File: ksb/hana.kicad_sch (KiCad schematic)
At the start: 19 parts, among them U4 X850744-001

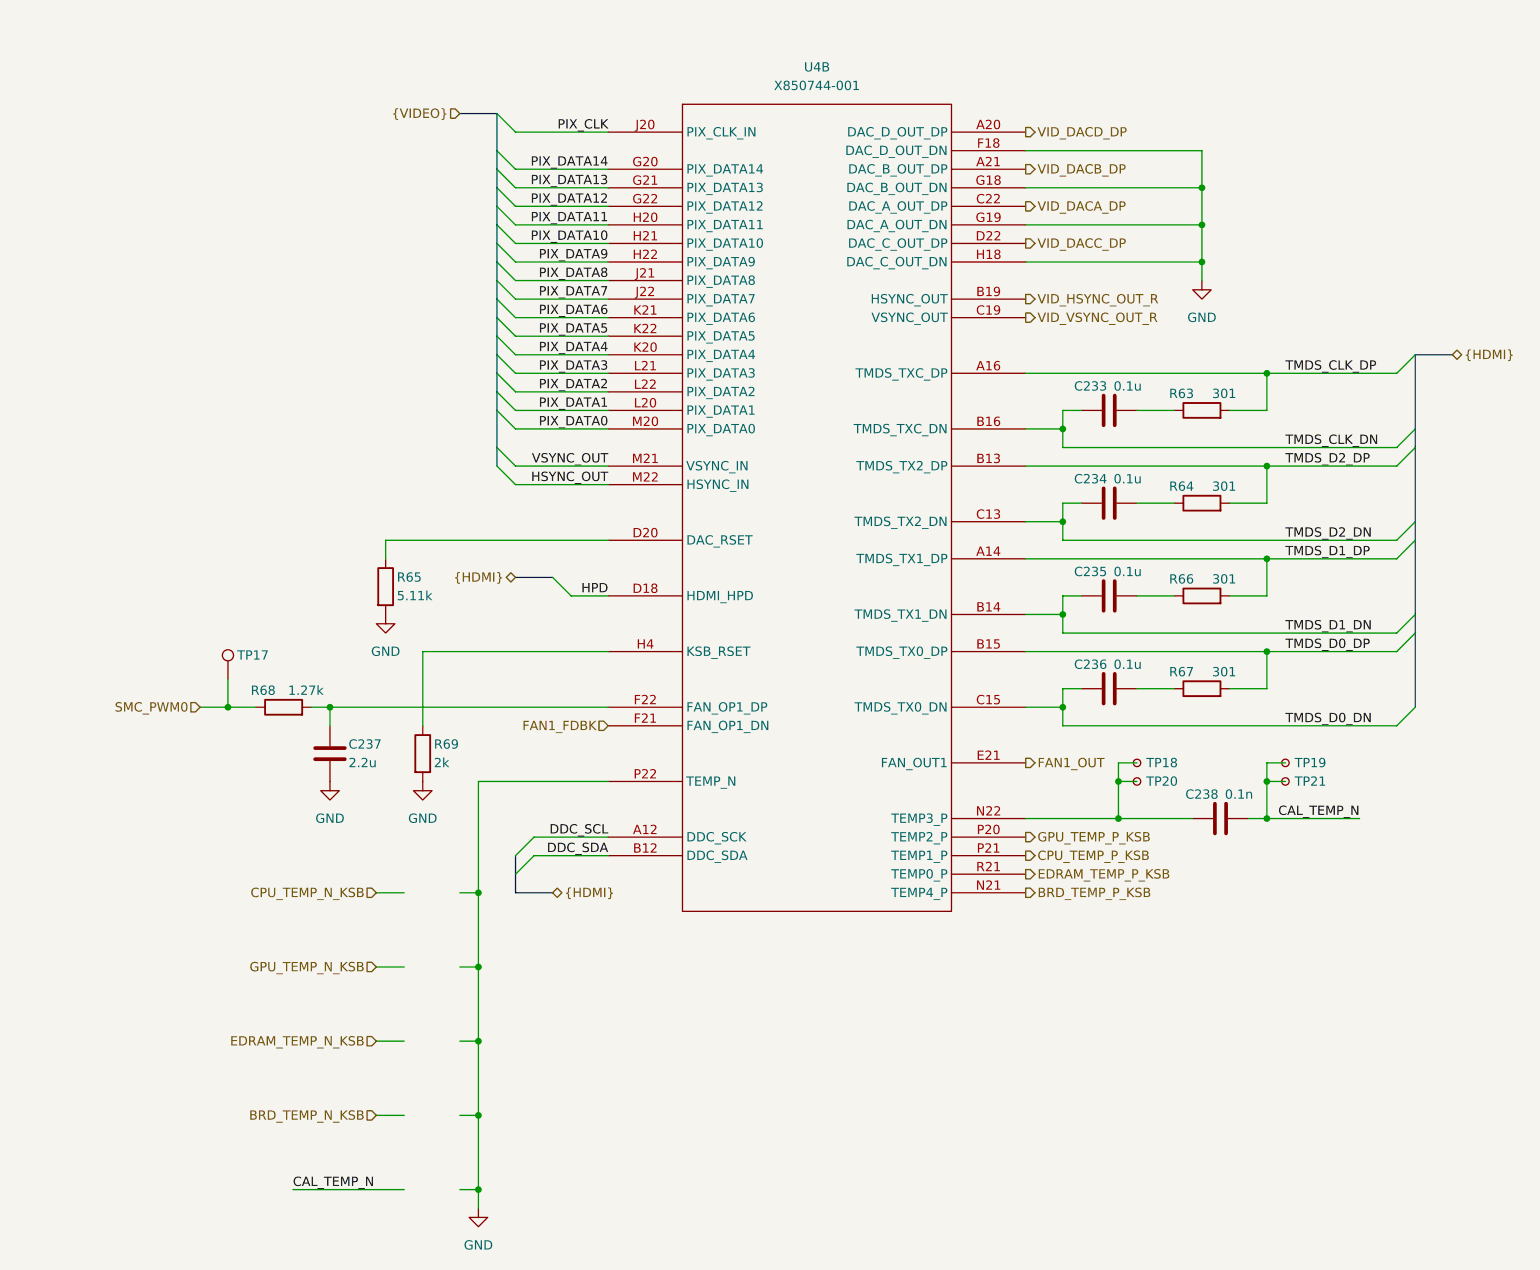
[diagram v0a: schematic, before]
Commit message: Cleanup, SMC GPIO connections and Temperature sensing
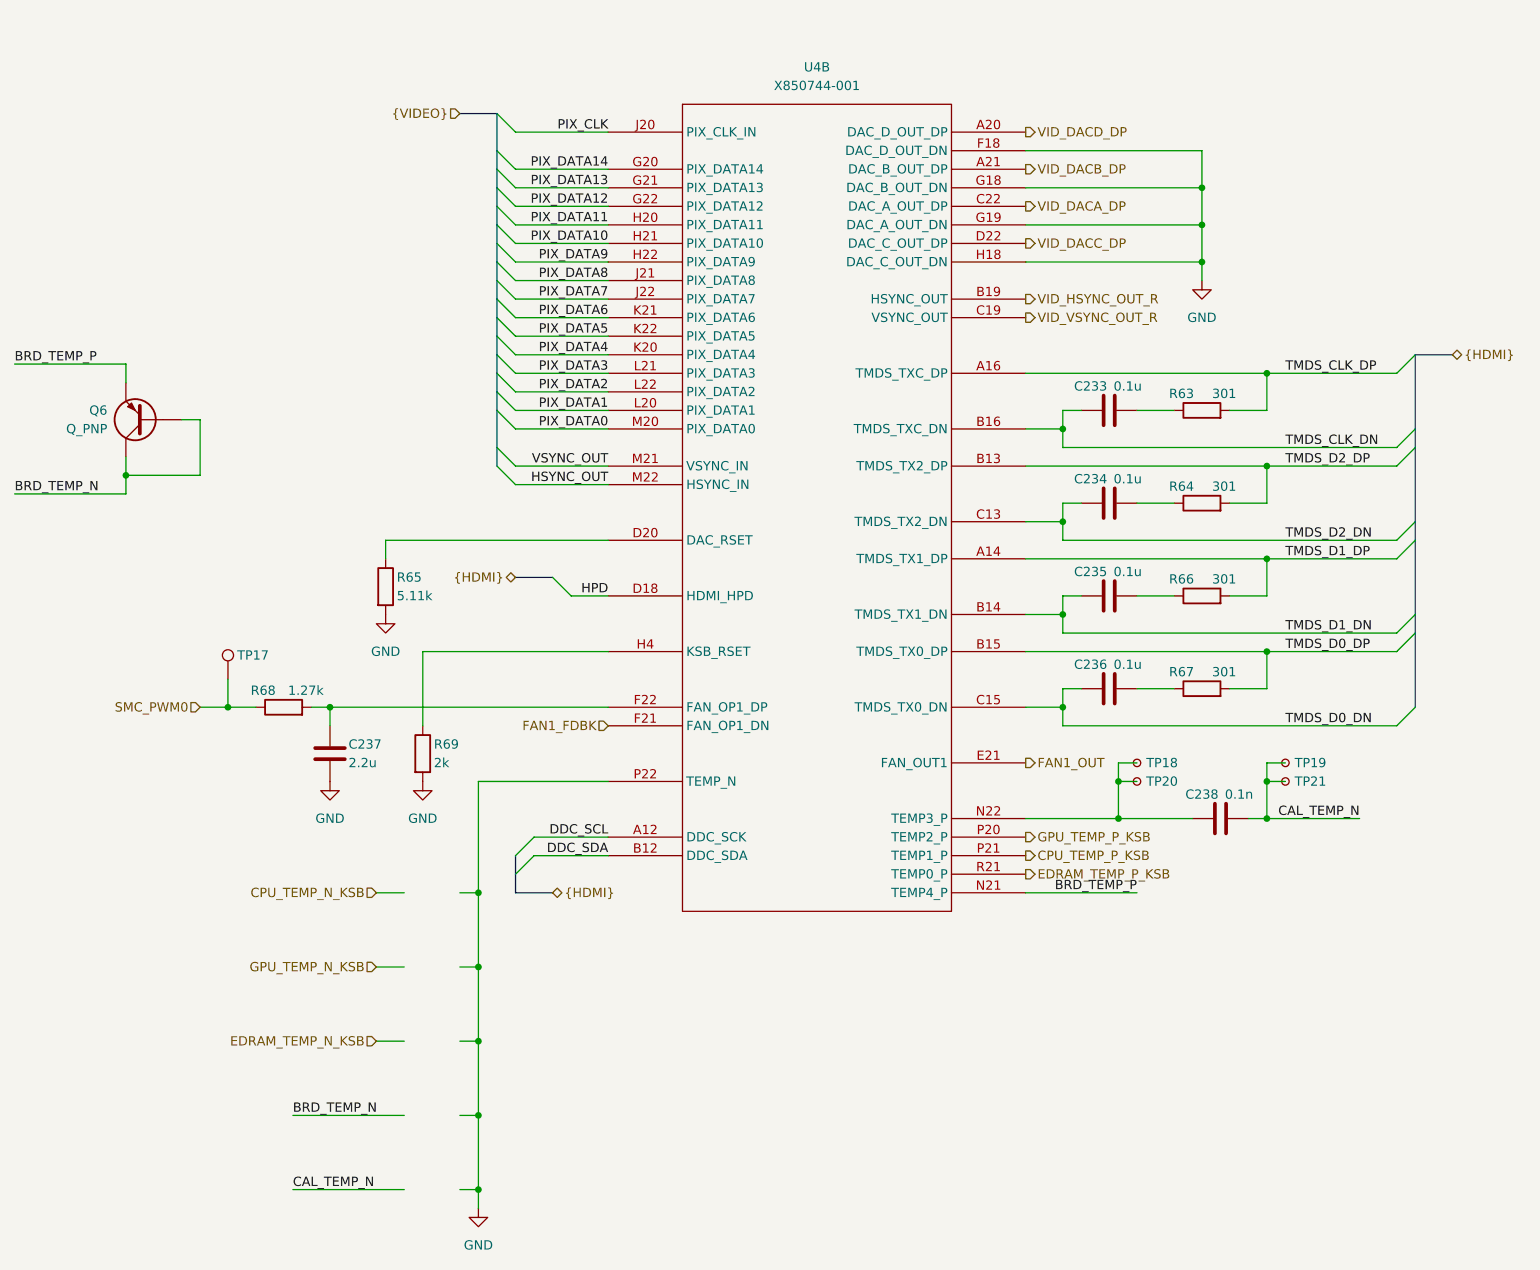
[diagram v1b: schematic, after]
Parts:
- added Q6: Q_PNP, symbol Device:Q_PNP
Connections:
- net BRD_TEMP_P_KSB renamed BRD_TEMP_P
- net BRD_TEMP_P: now also Q6.E
- new net BRD_TEMP_N: Q6.B, Q6.C
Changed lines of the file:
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@@
+	)
+	(junction
+		(at 53.34 80.01)
+		(diameter 0)
+		(color 0 0 0 0)
 	)
 	(junction
@@
 	(wire
 		(pts
-			(xy 87.63 167.64) (xy 91.44 167.64)
-		)
-		(stroke
-			(width 0)
-			(type default)
-		)
-	)
-	(wire
-		(pts
 			(xy 181.61 109.22) (xy 184.15 109.22)
 		)
@@
 	(wire
 		(pts
+			(xy 176.53 137.16) (xy 191.77 137.16)
+		)
+		(stroke
+			(width 0)
+			(type default)
+		)
+	)
+	(wire
+		(pts
 			(xy 209.55 121.92) (xy 212.09 121.92)
 		)
@@
 		)
 	)
+	(wire
+		(pts
+			(xy 53.34 64.77) (xy 53.34 67.31)
+		)
+		(stroke
+			(width 0)
+			(type default)
+		)
+	)
 	(bus
 		(pts
@@
 	(wire
 		(pts
+			(xy 76.2 167.64) (xy 91.44 167.64)
+		)
+		(stroke
+			(width 0)
+			(type default)
+		)
+	)
+	(wire
+		(pts
 			(xy 119.38 53.34) (xy 106.68 53.34)
 		)
@@
 		)
 	)
+	(wire
+		(pts
+			(xy 53.34 77.47) (xy 53.34 80.01)
+		)
+		(stroke
+			(width 0)
+			(type default)
+		)
+	)
 	(bus
 		(pts
@@
 	(wire
 		(pts
+			(xy 60.96 72.39) (xy 63.5 72.39)
+		)
+		(stroke
+			(width 0)
+			(type default)
+		)
+	)
+	(wire
+		(pts
 			(xy 63.5 111.76) (xy 67.31 111.76)
 		)
@@
 		)
 	)
+	(wire
+		(pts
+			(xy 53.34 64.77) (xy 38.1 64.77)
+		)
+		(stroke
+			(width 0)
+			(type default)
+		)
+	)
 	(bus
 		(pts
@@
 	(wire
 		(pts
+			(xy 63.5 80.01) (xy 53.34 80.01)
+		)
+		(stroke
+			(width 0)
+			(type default)
+		)
+	)
+	(wire
+		(pts
 			(xy 209.55 91.44) (xy 227.33 91.44)
 		)
@@
 	(wire
 		(pts
+			(xy 63.5 72.39) (xy 63.5 80.01)
+		)
+		(stroke
+			(width 0)
+			(type default)
+		)
+	)
+	(wire
+		(pts
 			(xy 209.55 121.92) (xy 209.55 127)
 		)
@@
 	(wire
 		(pts
+			(xy 38.1 82.55) (xy 53.34 82.55)
+		)
+		(stroke
+			(width 0)
+			(type default)
+		)
+	)
+	(wire
+		(pts
 			(xy 209.55 104.14) (xy 227.33 104.14)
 		)
@@
 		(pts
 			(xy 209.55 109.22) (xy 209.55 104.14)
+		)
+		(stroke
+			(width 0)
+			(type default)
+		)
+	)
+	(wire
+		(pts
+			(xy 53.34 80.01) (xy 53.34 82.55)
 		)
 		(stroke
@@
 		)
 	)
+	(label "BRD_TEMP_N"
+		(at 76.2 167.64 0)
+		(effects
+			(font
+				(size 1.27 1.27)
+			)
+			(justify left bottom)
+		)
+	)
 	(label "PIX_DATA7"
 		(at 119.38 55.88 180)
@@
 		)
 	)
+	(label "BRD_TEMP_P"
+		(at 191.77 137.16 180)
+		(effects
+			(font
+				(size 1.27 1.27)
+			)
+			(justify right bottom)
+		)
+	)
 	(label "PIX_DATA1"
 		(at 119.38 71.12 180)
@@
 		)
 	)
+	(label "BRD_TEMP_N"
+		(at 38.1 82.55 0)
+		(effects
+			(font
+				(size 1.27 1.27)
+			)
+			(justify left bottom)
+		)
+	)
 	(label "TMDS_D2_DN"
 		(at 212.09 88.9 0)
@@
 			)
 			(justify right bottom)
+		)
+	)
+	(label "BRD_TEMP_P"
+		(at 38.1 64.77 0)
+		(effects
+			(font
+				(size 1.27 1.27)
+			)
+			(justify left bottom)
 		)
 	)
@@
 		)
 	)
-	(hierarchical_label "BRD_TEMP_P_KSB"
-		(shape output)
-		(at 176.53 137.16 0)
-		(effects
-			(font
-				(size 1.27 1.27)
-			)
-			(justify left)
-		)
-	)
 	(hierarchical_label "VID_DACC_DP"
 		(shape output)
@@
 			)
 			(justify left)
-		)
-	)
-	(hierarchical_label "BRD_TEMP_N_KSB"
-		(shape input)
-		(at 87.63 167.64 180)
-		(effects
-			(font
-				(size 1.27 1.27)
-			)
-			(justify right)
 		)
 	)
@@
 					(unit 1)
 				)
+			)
+		)
+	)
+	(symbol
+		(lib_id "Device:Q_PNP")
+		(at 55.88 72.39 180)
+		(unit 1)
+		(exclude_from_sim no)
+		(in_bom yes)
+		(on_board yes)
+		(dnp no)
+		(property "Reference" "Q6"
+			(at 50.8 71.12 0)
+			(effects
+				(font
+					(size 1.27 1.27)
+				)
+				(justify left)
+			)
+		)
+		(property "Value" "Q_PNP"
+			(at 50.8 73.66 0)
+			(effects
+				(font
+					(size 1.27 1.27)
+				)
+				(justify left)
+			)
+		)
+		(property "Footprint" ""
+			(at 50.8 74.93 0)
+			(effects
+				(font
+					(size 1.27 1.27)
+				)
+				(hide yes)
+			)
+		)
+		(property "Datasheet" "~"
+			(at 55.88 72.39 0)
+			(effects
+				(font
+					(size 1.27 1.27)
+				)
+				(hide yes)
+			)
+		)
+		(property "Description" "PNP bipolar junction transistor"
+			(at 55.88 72.39 0)
+			(effects
+				(font
+					(size 1.27 1.27)
+				)
+				(hide yes)
+			)
+		)
+		(pin "B"
+		)
+		(pin "C"
+		)
+		(pin "E"
+		)
+		(instances
+			(project "Mantaray"
+				(path "/16640ecb-e4a4-4594-871b-70047bfba6e0/5578fb0d-7a85-48a3-97bd-11e67ac7c8dc/d6113545-4299-4788-b32a-3a696a198c82"
+					(reference "Q6")
+					(unit 1)
+				)

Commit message: Internal Connectors
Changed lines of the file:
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@@
+		)
+	)
+	(bus
+		(pts
+			(xy 104.14 27.94) (xy 104.14 30.48)
+		)
+		(stroke
+			(width 0)
+			(type default)
 		)
 	)
@@
 	(bus
 		(pts
-			(xy 106.68 93.98) (xy 111.76 93.98)
+			(xy 109.22 93.98) (xy 111.76 93.98)
 		)
 		(stroke
@@
 	(bus
 		(pts
+			(xy 229.87 60.96) (xy 229.87 63.5)
+		)
+		(stroke
+			(width 0)
+			(type default)
+		)
+	)
+	(bus
+		(pts
 			(xy 229.87 111.76) (xy 229.87 101.6)
 		)
@@
 		)
 	)
-	(bus
-		(pts
-			(xy 104.14 30.48) (xy 99.06 30.48)
-		)
-		(stroke
-			(width 0)
-			(type default)
-		)
-	)
 	(wire
 		(pts
@@
 		(pts
 			(xy 99.06 147.32) (xy 101.6 147.32)
-		)
-		(stroke
-			(width 0)
-			(type default)
-		)
-	)
-	(bus
-		(pts
-			(xy 106.68 137.16) (xy 111.76 137.16)
-		)
-		(stroke
-			(width 0)
-			(type default)
-		)
-	)
-	(bus
-		(pts
-			(xy 229.87 63.5) (xy 234.95 63.5)
 		)
 		(stroke
@@
 	(hierarchical_label "{HDMI}"
 		(shape bidirectional)
-		(at 111.76 137.16 0)
-		(effects
-			(font
-				(size 1.27 1.27)
-			)
-			(justify left)
+		(at 106.68 137.16 270)
+		(effects
+			(font
+				(size 1.27 1.27)
+			)
+			(justify right)
 		)
 	)
@@
 	(hierarchical_label "{VIDEO}"
 		(shape input)
-		(at 99.06 30.48 180)
-		(effects
-			(font
-				(size 1.27 1.27)
-			)
-			(justify right)
+		(at 104.14 27.94 90)
+		(effects
+			(font
+				(size 1.27 1.27)
+			)
+			(justify left)
 		)
 	)
 	(hierarchical_label "{HDMI}"
 		(shape bidirectional)
-		(at 106.68 93.98 180)
+		(at 109.22 93.98 180)
 		(effects
 			(font
@@
 	(hierarchical_label "{HDMI}"
 		(shape bidirectional)
-		(at 234.95 63.5 0)
-		(effects
-			(font
+		(at 229.87 60.96 90)
+		(effects
+			(font

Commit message: Cleanup & Debug I/O
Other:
- moved on the sheet: TP17
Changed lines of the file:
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@@
 	(paper "A4")
 	(junction
-		(at 200.66 45.72)
+		(at 199.39 45.72)
 		(diameter 0)
 		(color 0 0 0 0)
 	)
 	(junction
-		(at 200.66 50.8)
+		(at 199.39 50.8)
 		(diameter 0)
 		(color 0 0 0 0)
@@
 	)
 	(junction
-		(at 67.31 111.76)
+		(at 209.55 104.14)
 		(diameter 0)
 		(color 0 0 0 0)
 	)
 	(junction
-		(at 209.55 104.14)
+		(at 68.58 111.76)
 		(diameter 0)
 		(color 0 0 0 0)
 	)
 	(junction
-		(at 200.66 40.64)
+		(at 199.39 40.64)
 		(diameter 0)
 		(color 0 0 0 0)
@@
 	(wire
 		(pts
-			(xy 176.53 137.16) (xy 191.77 137.16)
+			(xy 176.53 137.16) (xy 189.23 137.16)
 		)
 		(stroke
@@
 	(wire
 		(pts
-			(xy 200.66 35.56) (xy 200.66 40.64)
+			(xy 199.39 35.56) (xy 199.39 40.64)
 		)
 		(stroke
@@
 	(wire
 		(pts
-			(xy 176.53 40.64) (xy 200.66 40.64)
+			(xy 176.53 40.64) (xy 199.39 40.64)
 		)
 		(stroke
@@
 	(wire
 		(pts
-			(xy 63.5 111.76) (xy 67.31 111.76)
+			(xy 66.04 111.76) (xy 68.58 111.76)
 		)
 		(stroke
@@
 	(wire
 		(pts
-			(xy 200.66 45.72) (xy 200.66 50.8)
+			(xy 199.39 45.72) (xy 199.39 50.8)
 		)
 		(stroke
@@
 	(wire
 		(pts
-			(xy 87.63 157.48) (xy 91.44 157.48)
+			(xy 88.9 157.48) (xy 91.44 157.48)
 		)
 		(stroke
@@
 	(wire
 		(pts
-			(xy 87.63 147.32) (xy 91.44 147.32)
+			(xy 88.9 147.32) (xy 91.44 147.32)
 		)
 		(stroke
@@
 	(wire
 		(pts
-			(xy 200.66 50.8) (xy 200.66 53.34)
+			(xy 199.39 50.8) (xy 199.39 53.34)
 		)
 		(stroke
@@
 	(wire
 		(pts
-			(xy 67.31 111.76) (xy 71.12 111.76)
-		)
-		(stroke
-			(width 0)
-			(type default)
-		)
-	)
-	(wire
-		(pts
 			(xy 119.38 81.28) (xy 106.68 81.28)
 		)
@@
 	(wire
 		(pts
+			(xy 68.58 111.76) (xy 71.12 111.76)
+		)
+		(stroke
+			(width 0)
+			(type default)
+		)
+	)
+	(wire
+		(pts
 			(xy 181.61 76.2) (xy 181.61 73.66)
 		)
@@
 	(wire
 		(pts
-			(xy 176.53 45.72) (xy 200.66 45.72)
+			(xy 176.53 45.72) (xy 199.39 45.72)
 		)
 		(stroke
@@
 	(wire
 		(pts
-			(xy 67.31 107.95) (xy 67.31 111.76)
+			(xy 68.58 109.22) (xy 68.58 111.76)
 		)
 		(stroke
@@
 	(wire
 		(pts
-			(xy 200.66 40.64) (xy 200.66 45.72)
+			(xy 199.39 40.64) (xy 199.39 45.72)
 		)
 		(stroke
@@
 	(wire
 		(pts
-			(xy 87.63 137.16) (xy 91.44 137.16)
+			(xy 88.9 137.16) (xy 91.44 137.16)
 		)
 		(stroke
@@
 	(wire
 		(pts
-			(xy 176.53 35.56) (xy 200.66 35.56)
+			(xy 176.53 35.56) (xy 199.39 35.56)
 		)
 		(stroke
@@
 	(wire
 		(pts
-			(xy 200.66 50.8) (xy 176.53 50.8)
+			(xy 199.39 50.8) (xy 176.53 50.8)
 		)
 		(stroke
@@
 	)
 	(label "BRD_TEMP_P"
-		(at 191.77 137.16 180)
+		(at 189.23 137.16 180)
 		(effects
 			(font
@@
 	(hierarchical_label "SMC_PWM0"
 		(shape input)
-		(at 63.5 111.76 180)
+		(at 66.04 111.76 180)
 		(effects
 			(font
@@
 	(hierarchical_label "EDRAM_TEMP_N_KSB"
 		(shape input)
-		(at 87.63 157.48 180)
+		(at 88.9 157.48 180)
 		(effects
 			(font
@@
 	(hierarchical_label "CPU_TEMP_N_KSB"
 		(shape input)
-		(at 87.63 137.16 180)
+		(at 88.9 137.16 180)
 		(effects
 			(font
@@
 	(hierarchical_label "GPU_TEMP_N_KSB"
 		(shape input)
-		(at 87.63 147.32 180)
+		(at 88.9 147.32 180)
 		(effects
 			(font
@@
 	(symbol
 		(lib_id "power:GND")
-		(at 200.66 53.34 0)
+		(at 199.39 53.34 0)
 		(unit 1)
 		(exclude_from_sim no)
@@
 		(fields_autoplaced yes)
 		(property "Reference" "#PWR0106"
-			(at 200.66 59.69 0)
+			(at 199.39 59.69 0)
 			(effects
 				(font
@@
 		)
 		(property "Value" "GND"
-			(at 200.66 58.42 0)
+			(at 199.39 58.42 0)
 			(effects
 				(font
@@
 		)
 		(property "Footprint" ""
-			(at 200.66 53.34 0)
+			(at 199.39 53.34 0)
 			(effects
 				(font
@@
 		)
 		(property "Datasheet" ""
-			(at 200.66 53.34 0)
+			(at 199.39 53.34 0)
 			(effects
 				(font
@@
 		)
 		(property "Description" "Power symbol creates a global label with name \"GND\" , ground"
-			(at 200.66 53.34 0)
+			(at 199.39 53.34 0)
 			(effects
 				(font
@@
 	(symbol
 		(lib_id "Connector:TestPoint")
-		(at 67.31 107.95 0)
+		(at 68.58 109.22 0)
 		(unit 1)
 		(exclude_from_sim no)
@@
 		(dnp no)
 		(property "Reference" "TP17"
-			(at 68.58 104.648 0)
+			(at 69.85 105.918 0)
 			(effects
 				(font
@@
 		)
 		(property "Value" "TestPoint"
-			(at 69.85 105.9179 0)
+			(at 71.12 107.1879 0)
 			(effects
 				(font
@@
 		)
 		(property "Footprint" ""
-			(at 72.39 107.95 0)
+			(at 73.66 109.22 0)
 			(effects
 				(font
@@
 		)
 		(property "Datasheet" "~"
-			(at 72.39 107.95 0)
+			(at 73.66 109.22 0)
 			(effects
 				(font
@@
 		)
 		(property "Description" "test point"
-			(at 67.31 107.95 0)
+			(at 68.58 109.22 0)
 			(effects
 				(font

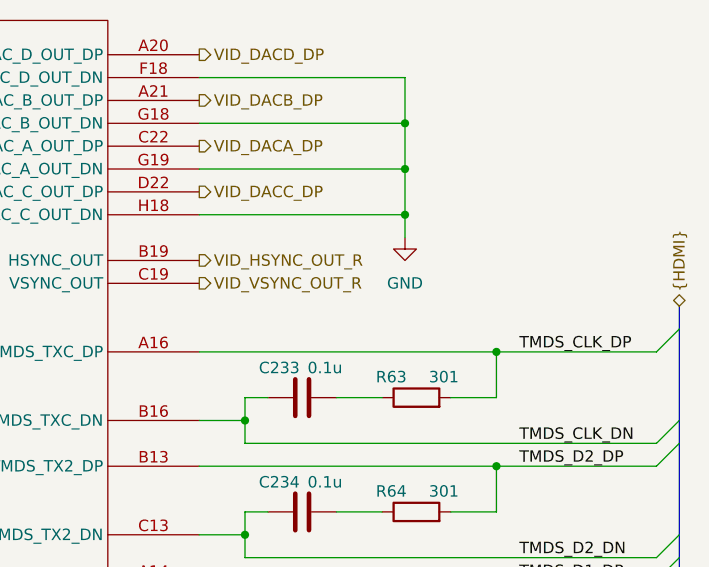
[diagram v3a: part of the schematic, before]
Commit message: Audio Output, Analog isolation and TOSLINK
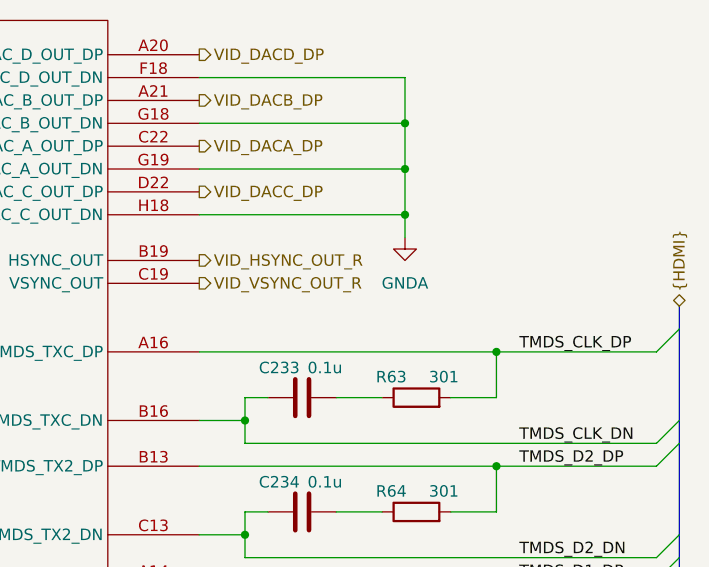
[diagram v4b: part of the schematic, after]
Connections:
- net GND: no longer U4.F18 (DAC_D_OUT_DN), U4.G18 (DAC_B_OUT_DN), U4.G19 (DAC_A_OUT_DN), U4.H18 (DAC_C_OUT_DN)
- new net GNDA: U4.F18 (DAC_D_OUT_DN), U4.G18 (DAC_B_OUT_DN), U4.G19 (DAC_A_OUT_DN), U4.H18 (DAC_C_OUT_DN)
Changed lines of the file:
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@@
-	)
-	(symbol
-		(lib_id "power:GND")
-		(at 199.39 53.34 0)
-		(unit 1)
-		(exclude_from_sim no)
-		(in_bom yes)
-		(on_board yes)
-		(dnp no)
-		(fields_autoplaced yes)
-		(property "Reference" "#PWR0106"
-			(at 199.39 59.69 0)
-			(effects
-				(font
-					(size 1.27 1.27)
-				)
-				(hide yes)
-			)
-		)
-		(property "Value" "GND"
-			(at 199.39 58.42 0)
-			(effects
-				(font
-					(size 1.27 1.27)
-				)
-			)
-		)
-		(property "Footprint" ""
-			(at 199.39 53.34 0)
-			(effects
-				(font
-					(size 1.27 1.27)
-				)
-				(hide yes)
-			)
-		)
-		(property "Datasheet" ""
-			(at 199.39 53.34 0)
-			(effects
-				(font
-					(size 1.27 1.27)
-				)
-				(hide yes)
-			)
-		)
-		(property "Description" "Power symbol creates a global label with name \"GND\" , ground"
-			(at 199.39 53.34 0)
-			(effects
-				(font
-					(size 1.27 1.27)
-				)
-				(hide yes)
-			)
-		)
-		(pin "1"
-		)
-		(instances
-			(project "StingBurst"
-				(path "/16640ecb-e4a4-4594-871b-70047bfba6e0/5578fb0d-7a85-48a3-97bd-11e67ac7c8dc/d6113545-4299-4788-b32a-3a696a198c82"
-					(reference "#PWR0106")
-					(unit 1)
-				)
-			)
-		)
 	)
 	(symbol
@@
 					(unit 1)
 				)
+			)
+		)
+	)
+	(symbol
+		(lib_id "power:GNDA")
+		(at 199.39 53.34 0)
+		(unit 1)
+		(exclude_from_sim no)
+		(in_bom yes)
+		(on_board yes)
+		(dnp no)
+		(fields_autoplaced yes)
+		(property "Reference" "#PWR0214"
+			(at 199.39 59.69 0)
+			(effects
+				(font
+					(size 1.27 1.27)
+				)
+				(hide yes)
+			)
+		)
+		(property "Value" "GNDA"
+			(at 199.39 58.42 0)
+			(effects
+				(font
+					(size 1.27 1.27)
+				)
+			)
+		)
+		(property "Footprint" ""
+			(at 199.39 53.34 0)
+			(effects
+				(font
+					(size 1.27 1.27)
+				)
+				(hide yes)
+			)
+		)
+		(property "Datasheet" ""
+			(at 199.39 53.34 0)
+			(effects
+				(font
+					(size 1.27 1.27)
+				)
+				(hide yes)
+			)
+		)
+		(property "Description" "Power symbol creates a global label with name \"GNDA\" , analog ground"
+			(at 199.39 53.34 0)
+			(effects
+				(font
+					(size 1.27 1.27)
+				)
+				(hide yes)
+			)
+		)
+		(pin "1"
+		)
+		(instances
+			(project ""
+				(path "/16640ecb-e4a4-4594-871b-70047bfba6e0/5578fb0d-7a85-48a3-97bd-11e67ac7c8dc/d6113545-4299-4788-b32a-3a696a198c82"
+					(reference "#PWR0214")
+					(unit 1)
+				)
